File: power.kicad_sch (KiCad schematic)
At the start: 34 parts, among them J12 AREF-TEST/MODULE, J14 Power DC 5V, J4 5V, J8 Power Route, U4 AMS1117-3.3

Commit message: Add AGND capacitors
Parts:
- added C21: 10nF, Capacitor_SMD:C_0805_2012Metric, symbol Device:C
- added C22: 100nF, Capacitor_SMD:C_0805_2012Metric, symbol Device:C
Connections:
- net AGND: now also C21.1, C22.1
- net AVCC: now also C21.2, C22.2

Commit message: Update APower
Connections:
- net AGND: now also C17.2
- net GND1: no longer C17.2
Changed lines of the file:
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@@
+	)
+	(junction
+		(at 185.42 99.06)
+		(diameter 0)
+		(color 0 0 0 0)
 	)
 	(junction
@@
 	)
 	(junction
-		(at 163.83 99.06)
-		(diameter 0)
-		(color 0 0 0 0)
-	)
-	(junction
 		(at 185.42 116.84)
 		(diameter 0)
@@
 	)
 	(junction
-		(at 153.67 99.06)
-		(diameter 0)
-		(color 0 0 0 0)
-	)
-	(junction
 		(at 153.67 57.15)
 		(diameter 0)
@@
 	(wire
 		(pts
-			(xy 153.67 99.06) (xy 148.59 99.06)
-		)
-		(stroke
-			(width 0)
-			(type default)
-		)
-	)
-	(wire
-		(pts
 			(xy 59.69 128.27) (xy 55.88 128.27)
 		)
@@
 	(wire
 		(pts
+			(xy 185.42 99.06) (xy 189.23 99.06)
+		)
+		(stroke
+			(width 0)
+			(type default)
+		)
+	)
+	(wire
+		(pts
 			(xy 148.59 76.2) (xy 163.83 76.2)
 		)
@@
 	(wire
 		(pts
+			(xy 148.59 99.06) (xy 153.67 99.06)
+		)
+		(stroke
+			(width 0)
+			(type default)
+		)
+	)
+	(wire
+		(pts
 			(xy 119.38 148.59) (xy 113.03 148.59)
 		)
@@
 	(wire
 		(pts
-			(xy 163.83 99.06) (xy 153.67 99.06)
-		)
-		(stroke
-			(width 0)
-			(type default)
-		)
-	)
-	(wire
-		(pts
 			(xy 121.92 40.64) (xy 127 40.64)
 		)
@@
 		)
 	)
+	(global_label "GND1"
+		(shape input)
+		(at 189.23 99.06 0)
+		(fields_autoplaced yes)
+		(effects
+			(font
+				(size 1.27 1.27)
+			)
+			(justify left)
+		)
+		(property "Intersheetrefs" "${INTERSHEET_REFS}"
+			(at 197.2952 99.06 0)
+			(effects
+				(font
+					(size 1.27 1.27)
+				)
+				(justify left)
+				(hide yes)
+			)
+		)
+	)
 	(global_label "AREF"
 		(shape input)
@@
 		)
 	)
+	(global_label "AGND"
+		(shape input)
+		(at 148.59 99.06 180)
+		(fields_autoplaced yes)
+		(effects
+			(font
+				(size 1.27 1.27)
+			)
+			(justify right)
+		)
+		(property "Intersheetrefs" "${INTERSHEET_REFS}"
+			(at 140.6457 99.06 0)
+			(effects
+				(font
+					(size 1.27 1.27)
+				)
+				(justify right)
+				(hide yes)
+			)
+		)
+	)
 	(global_label "GND1"
 		(shape input)
@@
 			(effects
 				(font
-					(size 1.27 1.27)
-				)
-				(justify right)
-				(hide yes)
-			)
-		)
-	)
-	(global_label "GND1"
-		(shape input)
-		(at 148.59 99.06 180)
-		(fields_autoplaced yes)
-		(effects
-			(font
-				(size 1.27 1.27)
-			)
-			(justify right)
-		)
-		(property "Intersheetrefs" "${INTERSHEET_REFS}"
-			(at 140.5248 99.06 0)
-			(effects
-				(font

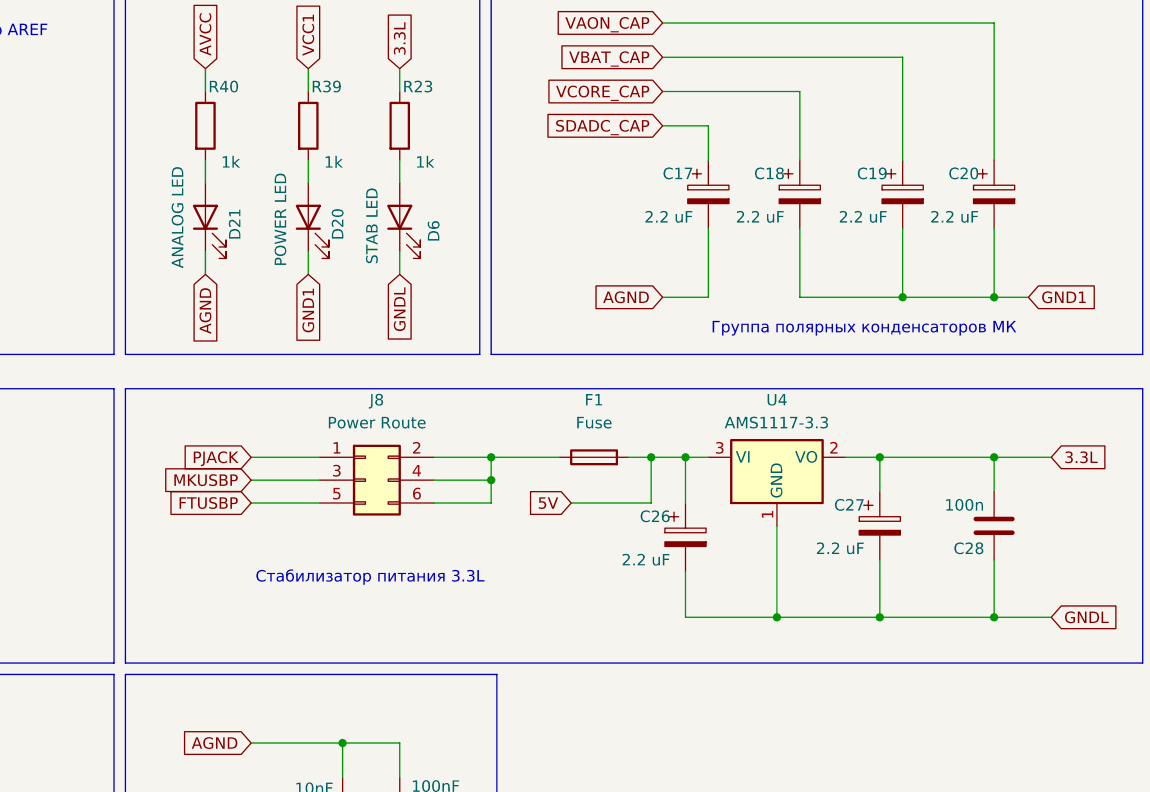
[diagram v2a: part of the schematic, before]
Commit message: Питание 5V от JTAG, множественные исправления
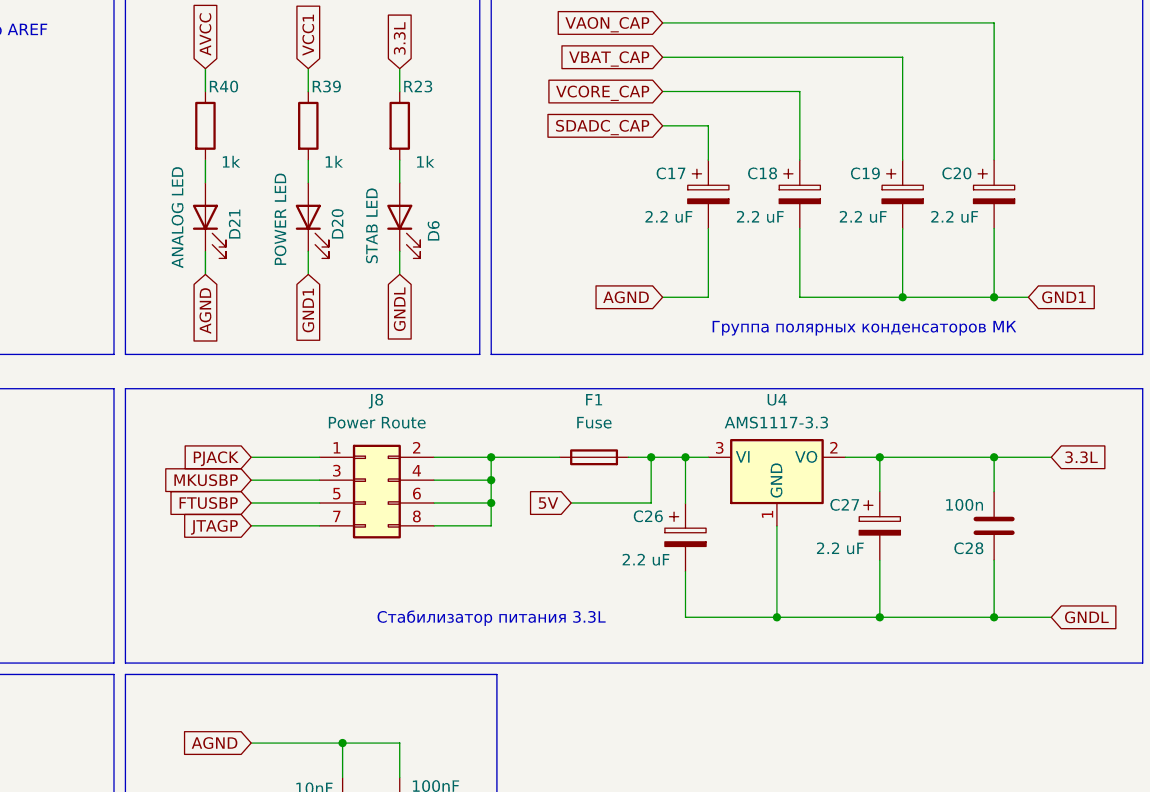
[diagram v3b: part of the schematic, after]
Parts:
- removed J8: Power Route, Connector_PinHeader_2.54mm:PinHeader_2x03_P2.54mm_Vertical, symbol Connector_Generic:Conn_02x03_Odd_Even
- added J8: Power Route, Connector_PinHeader_2.54mm:PinHeader_2x04_P2.54mm_Vertical, symbol Connector_Generic:Conn_02x04_Odd_Even
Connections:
- net FTUSBP: now also J8.5 (Pin_5)
- net MKUSBP: now also J8.3 (Pin_3)
- net PJACK: now also J8.1 (Pin_1)
- net at F1.1: now also J8.2 (Pin_2), J8.4 (Pin_4), J8.6 (Pin_6), J8.8 (Pin_8)
- new net JTAGP: J8.7 (Pin_7)
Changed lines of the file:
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@@
 	(text "Стабилизатор питания 3.3L"
 		(exclude_from_sim no)
-		(at 116.078 130.302 0)
+		(at 129.54 134.874 0)
 		(effects
 			(font
@@
 	)
 	(junction
+		(at 129.54 121.92)
+		(diameter 0)
+		(color 0 0 0 0)
+	)
+	(junction
 		(at 191.77 34.29)
 		(diameter 0)
@@
 	(wire
 		(pts
+			(xy 123.19 124.46) (xy 129.54 124.46)
+		)
+		(stroke
+			(width 0)
+			(type default)
+		)
+	)
+	(wire
+		(pts
 			(xy 151.13 116.84) (xy 153.67 116.84)
 		)
@@
 	(wire
 		(pts
+			(xy 129.54 124.46) (xy 129.54 121.92)
+		)
+		(stroke
+			(width 0)
+			(type default)
+		)
+	)
+	(wire
+		(pts
 			(xy 198.12 34.29) (xy 191.77 34.29)
 		)
@@
 	(wire
 		(pts
+			(xy 102.87 124.46) (xy 110.49 124.46)
+		)
+		(stroke
+			(width 0)
+			(type default)
+		)
+	)
+	(wire
+		(pts
 			(xy 119.38 148.59) (xy 113.03 148.59)
 		)
@@
 		)
 	)
+	(global_label "JTAGP"
+		(shape input)
+		(at 102.87 124.46 180)
+		(fields_autoplaced yes)
+		(effects
+			(font
+				(size 1.27 1.27)
+			)
+			(justify right)
+		)
+		(property "Intersheetrefs" "${INTERSHEET_REFS}"
+			(at 94.321 124.46 0)
+			(effects
+				(font
+					(size 1.27 1.27)
+				)
+				(justify right)
+				(hide yes)
+			)
+		)
+	)
 	(symbol
 		(lib_id "Device:C")
@@
 		(dnp no)
 		(property "Reference" "C26"
-			(at 146.05 123.444 0)
+			(at 145.288 123.444 0)
 			(effects
 				(font
@@
 		(dnp no)
 		(property "Reference" "C19"
-			(at 170.18 85.344 0)
+			(at 169.418 85.344 0)
 			(effects
 				(font
@@
 		(dnp no)
 		(property "Reference" "C18"
-			(at 158.75 85.344 0)
+			(at 157.988 85.344 0)
 			(effects
 				(font
@@
 		(dnp no)
 		(property "Reference" "C27"
-			(at 167.64 122.174 0)
+			(at 167.132 122.174 0)
 			(effects
 				(font
@@
 		(dnp no)
 		(property "Reference" "C17"
-			(at 148.59 85.344 0)
+			(at 147.828 85.344 0)
 			(effects
 				(font
@@
 		(dnp no)
 		(property "Reference" "C20"
-			(at 180.34 85.344 0)
+			(at 179.578 85.344 0)
 			(effects
 				(font
@@
 	)
 	(symbol
-		(lib_id "Connector_Generic:Conn_02x03_Odd_Even")
+		(lib_id "Connector_Generic:Conn_02x04_Odd_Even")
 		(at 115.57 119.38 0)
 		(unit 1)
@@
 			)
 		)
-		(property "Footprint" "Connector_PinHeader_2.54mm:PinHeader_2x03_P2.54mm_Vertical"
+		(property "Footprint" "Connector_PinHeader_2.54mm:PinHeader_2x04_P2.54mm_Vertical"
 			(at 115.57 119.38 0)
 			(effects
@@
 			)
 		)
-		(property "Description" "Generic connector, double row, 02x03, odd/even pin numbering scheme (row 1 odd numbers, row 2 even numbers), script generated (kicad-library-utils/schlib/autogen/connector/)"
+		(property "Description" "Generic connector, double row, 02x04, odd/even pin numbering scheme (row 1 odd numbers, row 2 even numbers), script generated (kicad-library-utils/schlib/autogen/connector/)"
 			(at 115.57 119.38 0)
 			(effects
@@
 			)
 		)
-		(pin "2"
-		)
-		(pin "4"
+		(pin "3"
 		)
-		(pin "6"
+		(pin "5"
 		)
-		(pin "3"
+		(pin "7"
 		)
 		(pin "1"
 		)
-		(pin "5"
+		(pin "4"
+		)
+		(pin "8"
+		)
+		(pin "6"
+		)
+		(pin "2"
 		)
 		(instances
-			(project "К1921ВГ015"
+			(project ""
 				(path "/bfe388ae-d75c-4df9-99dc-869f7637df55/7fe5bf4c-3a5d-4f52-9b61-54539d143c67"
 					(reference "J8")
